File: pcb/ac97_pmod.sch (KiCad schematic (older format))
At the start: 0 parts

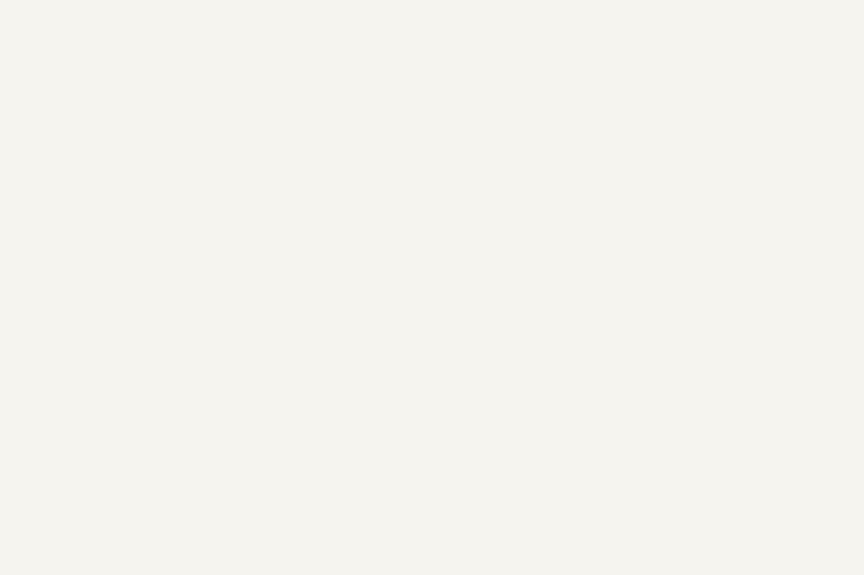
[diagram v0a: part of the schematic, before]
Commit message: replaced ceramic DC blocking caps with electrolytics
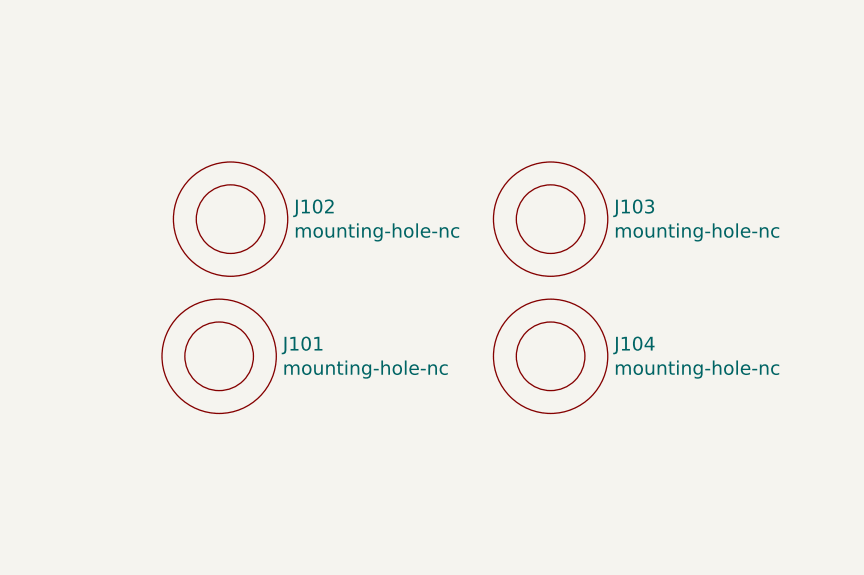
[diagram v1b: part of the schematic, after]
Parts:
- added J101, J102, J103, J104: mounting-hole-nc, wbraun_smd:M3-small-mounting-hole, symbol mounting-hole-nc
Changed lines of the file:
@@
-EESchema Schematic File Version 2
+EESchema Schematic File Version 3
 LIBS:power
 LIBS:device
@@
 LIBS:wbraun_ic_lib
 LIBS:ac97_pmod-cache
-EELAYER 25 0
+EELAYER 26 0
 EELAYER END
 $Descr A4 11693 8268
@@
 Wire Wire Line
 	3300 4400 2800 4400
+$Comp
+L mounting-hole-nc J102
+U 1 1 59FC94A8
+P 6600 3100
+F 0 "J102" H 6878 3153 60  0000 L CNN
+F 1 "mounting-hole-nc" H 6878 3047 60  0000 L CNN
+F 2 "wbraun_smd:M3-small-mounting-hole" H 6600 3100 60  0001 C CNN
+F 3 "" H 6600 3100 60  0001 C CNN
+	1    6600 3100
+	1    0    0    -1
+$EndComp
+$Comp
+L mounting-hole-nc J103
+U 1 1 59FC960F
+P 8000 3100
+F 0 "J103" H 8278 3153 60  0000 L CNN
+F 1 "mounting-hole-nc" H 8278 3047 60  0000 L CNN
+F 2 "wbraun_smd:M3-small-mounting-hole" H 8000 3100 60  0001 C CNN
+F 3 "" H 8000 3100 60  0001 C CNN
+	1    8000 3100
+	1    0    0    -1
+$EndComp
+$Comp
+L mounting-hole-nc J101
+U 1 1 59FC970B
+P 6550 3700
+F 0 "J101" H 6828 3753 60  0000 L CNN
+F 1 "mounting-hole-nc" H 6828 3647 60  0000 L CNN
+F 2 "wbraun_smd:M3-small-mounting-hole" H 6550 3700 60  0001 C CNN
+F 3 "" H 6550 3700 60  0001 C CNN
+	1    6550 3700
+	1    0    0    -1
+$EndComp
+$Comp
+L mounting-hole-nc J104
+U 1 1 59FC97B8
+P 8000 3700
+F 0 "J104" H 8278 3753 60  0000 L CNN
+F 1 "mounting-hole-nc" H 8278 3647 60  0000 L CNN
+F 2 "wbraun_smd:M3-small-mounting-hole" H 8000 3700 60  0001 C CNN
+F 3 "" H 8000 3700 60  0001 C CNN
+	1    8000 3700
+	1    0    0    -1
+$EndComp
 $EndSCHEMATC

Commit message: fixed bad schematic symbols due to new kicad version
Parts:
- removed J101: mounting-hole-nc, wbraun_smd:M3-small-mounting-hole, symbol mounting-hole-nc
- J102, J103, J104: symbol mounting-hole-nc -> ac97_pmod-rescue:mounting-hole-nc-RESCUE-ac97_pmod
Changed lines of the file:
@@
-EESchema Schematic File Version 3
-LIBS:power
-LIBS:device
-LIBS:transistors
-LIBS:conn
-LIBS:linear
-LIBS:regul
-LIBS:74xx
-LIBS:cmos4000
-LIBS:adc-dac
-LIBS:memory
-LIBS:xilinx
-LIBS:microcontrollers
-LIBS:dsp
-LIBS:microchip
-LIBS:analog_switches
-LIBS:motorola
-LIBS:texas
-LIBS:intel
-LIBS:audio
-LIBS:interface
-LIBS:digital-audio
-LIBS:philips
-LIBS:display
-LIBS:cypress
-LIBS:siliconi
-LIBS:opto
-LIBS:atmel
-LIBS:contrib
-LIBS:valves
-LIBS:wbraun_ic_lib
+EESchema Schematic File Version 4
 LIBS:ac97_pmod-cache
 EELAYER 26 0
@@
 	3300 4400 2800 4400
 $Comp
-L mounting-hole-nc J102
+L ac97_pmod-rescue:mounting-hole-nc-RESCUE-ac97_pmod J102
 U 1 1 59FC94A8
 P 6600 3100
@@
 $EndComp
 $Comp
-L mounting-hole-nc J103
+L ac97_pmod-rescue:mounting-hole-nc-RESCUE-ac97_pmod J103
 U 1 1 59FC960F
 P 8000 3100
@@
 $EndComp
 $Comp
-L mounting-hole-nc J101
-U 1 1 59FC970B
-P 6550 3700
-F 0 "J101" H 6828 3753 60  0000 L CNN
-F 1 "mounting-hole-nc" H 6828 3647 60  0000 L CNN
-F 2 "wbraun_smd:M3-small-mounting-hole" H 6550 3700 60  0001 C CNN
-F 3 "" H 6550 3700 60  0001 C CNN
-	1    6550 3700
-	1    0    0    -1
-$EndComp
-$Comp
-L mounting-hole-nc J104
+L ac97_pmod-rescue:mounting-hole-nc-RESCUE-ac97_pmod J104
 U 1 1 59FC97B8
 P 8000 3700
